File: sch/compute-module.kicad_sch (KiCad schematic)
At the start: 8 parts, among them J1 Conn_02x20_Odd_Even, J3 Conn_02x07_Odd_Even, SW1 SW_Push

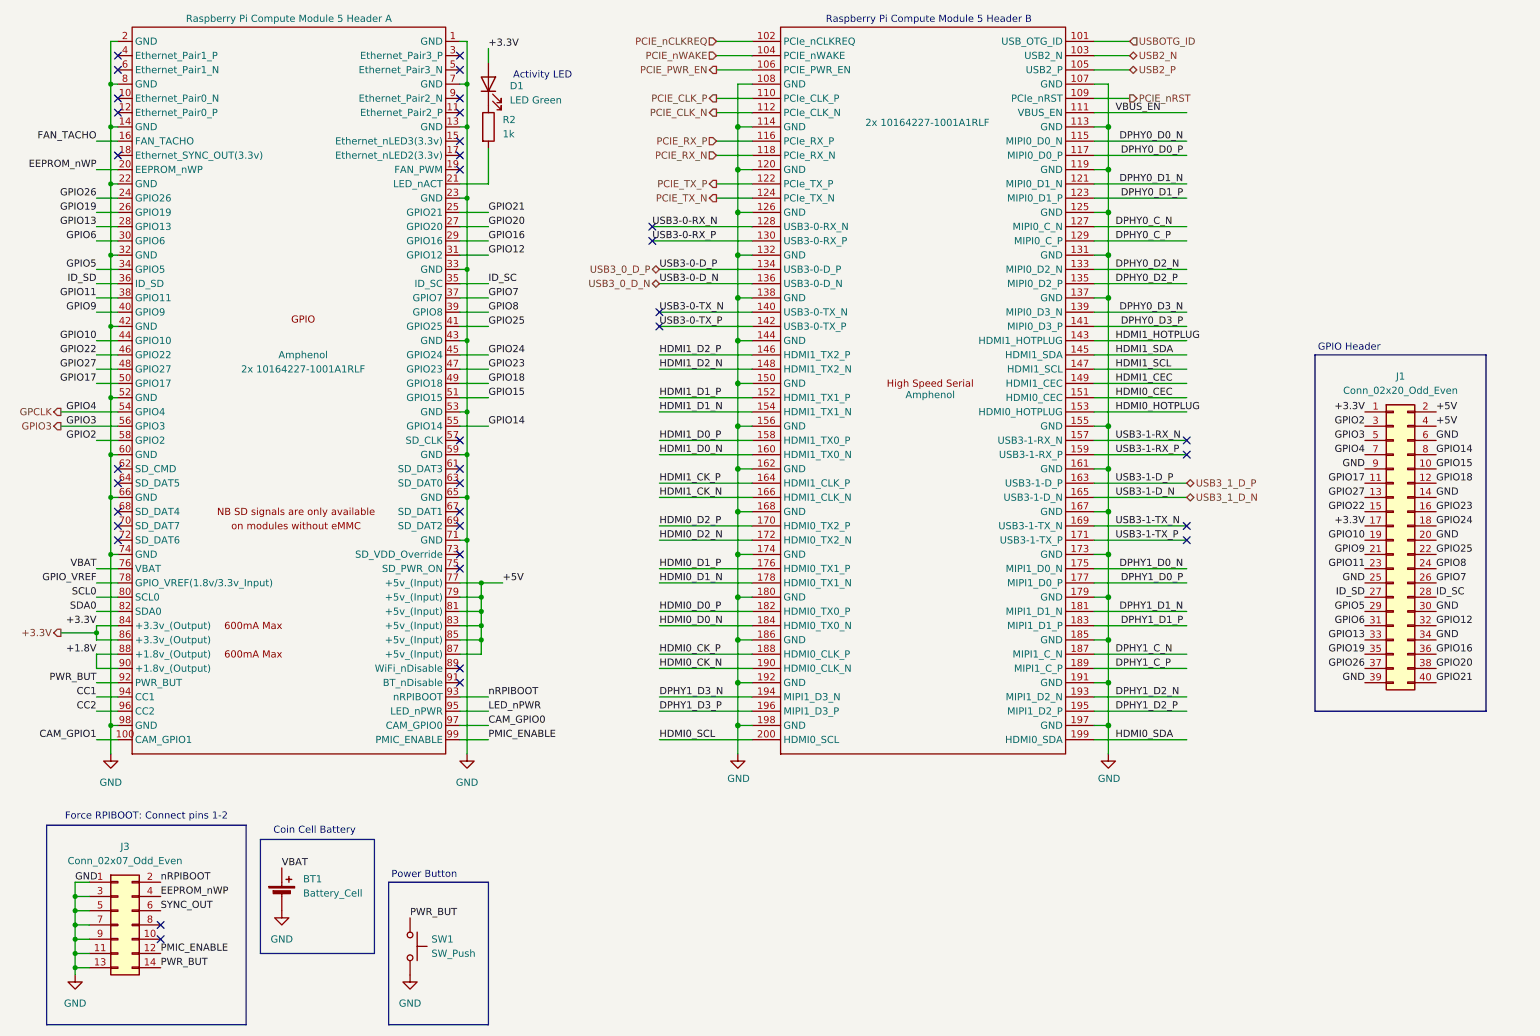
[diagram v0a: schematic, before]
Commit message: Connected pins between modem and CM5
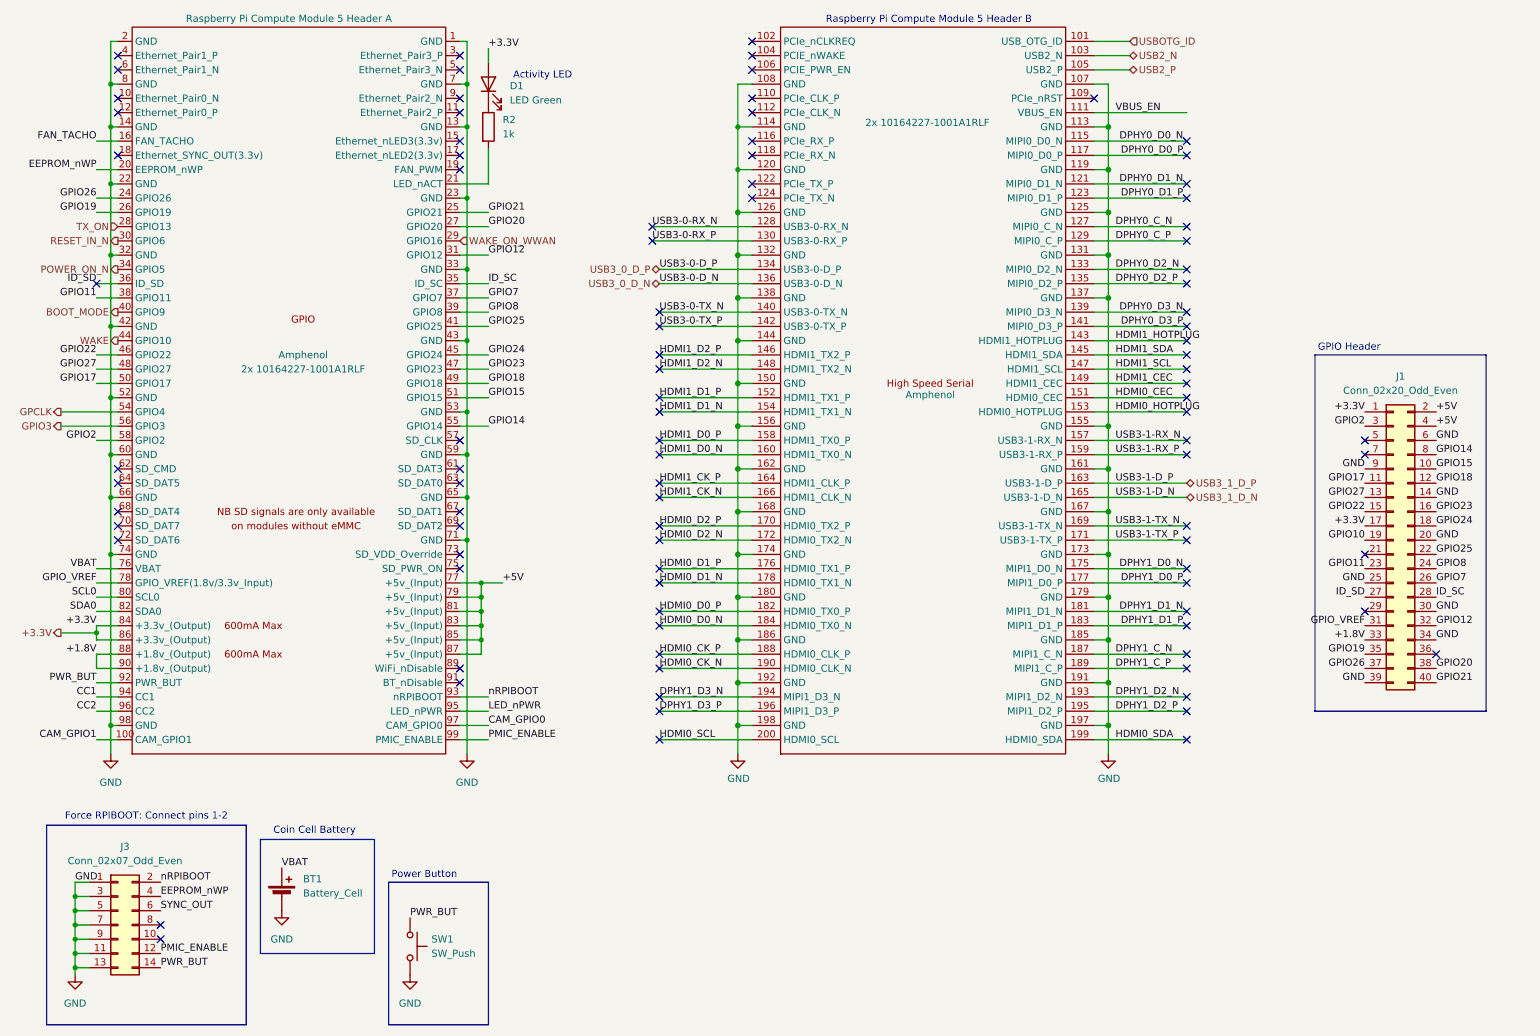
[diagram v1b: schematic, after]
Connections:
- net +1.8V: now also J1.33 (Pin_33)
- net GPCLK: no longer J1.7 (Pin_7)
- net GPIO10: no longer Module1.44 (GPIO10)
- net GPIO3: no longer J1.5 (Pin_5)
- net GPIO_VREF: now also J1.31 (Pin_31)
- net GPIO13 renamed TX_ON
- net TX_ON: no longer J1.33 (Pin_33)
- net GPIO16: no longer names the net of J1.36 (Pin_36)
- net GPIO16: no longer Module1.29 (GPIO16)
- net GPIO5: no longer names the net of J1.29 (Pin_29)
- net GPIO5: no longer Module1.34 (GPIO5)
- net GPIO6 renamed RESET_IN_N
- net RESET_IN_N: no longer J1.31 (Pin_31)
- net GPIO9: no longer names the net of J1.21 (Pin_21)
- net GPIO9: no longer Module1.40 (GPIO9)
- net PCIE_CLK_N: no longer names the net of Module2.112 (PCIe_CLK_N)
- net PCIE_CLK_P: no longer names the net of Module2.110 (PCIe_CLK_P)
- net PCIE_PWR_EN: no longer names the net of Module2.106 (PCIE_PWR_EN)
- net PCIE_RX_N: no longer names the net of Module2.118 (PCIe_RX_N)
- net PCIE_RX_P: no longer names the net of Module2.116 (PCIe_RX_P)
- net PCIE_TX_N: no longer names the net of Module2.124 (PCIe_TX_N)
- net PCIE_TX_P: no longer names the net of Module2.122 (PCIe_TX_P)
- net PCIE_nCLKREQ: no longer names the net of Module2.102 (PCIe_nCLKREQ)
- net PCIE_nRST: no longer names the net of Module2.109 (PCIe_nRST)
- net PCIE_nWAKE: no longer names the net of Module2.104 (PCIE_nWAKE)
- new net BOOT_MODE: Module1.40 (GPIO9)
- new net POWER_ON_N: Module1.34 (GPIO5)
- new net WAKE: Module1.44 (GPIO10)
- new net WAKE_ON_WWAN: Module1.29 (GPIO16)
- no-connect marks 36 -> 96

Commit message: Removed pin USBOTG
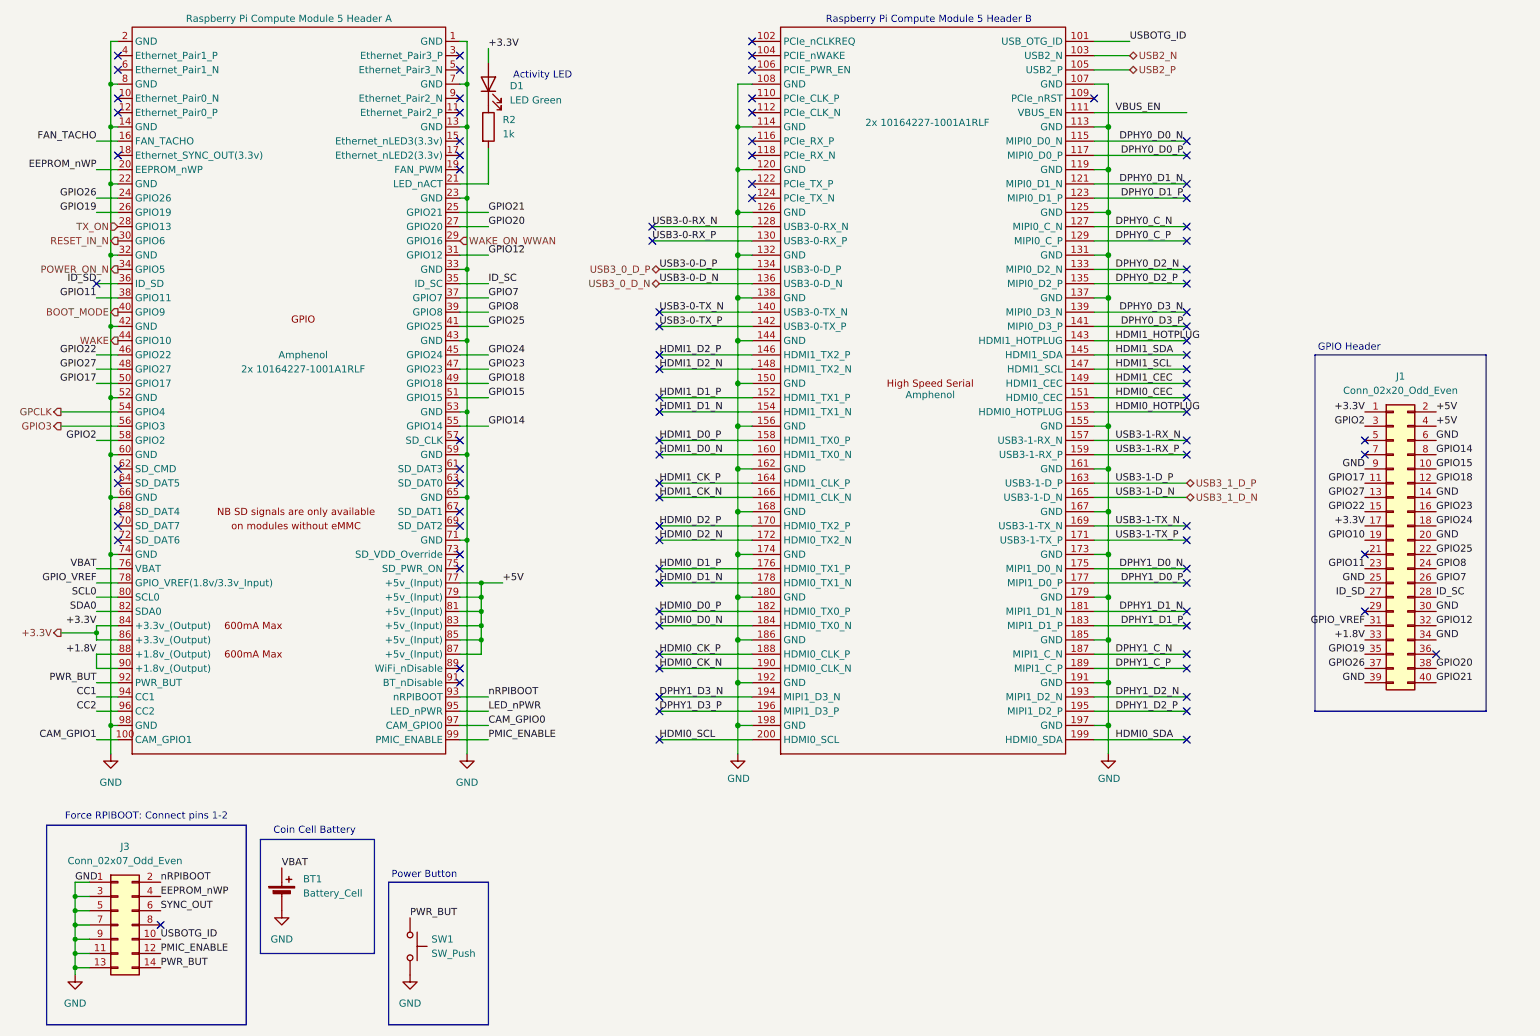
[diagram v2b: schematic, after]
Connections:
- net USBOTG_ID: now also J3.10 (Pin_10)
- no-connect marks 96 -> 95
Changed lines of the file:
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@@
 	)
 	(no_connect
-		(at 38.1 180.34)
-	)
-	(no_connect
 		(at 220.98 91.44)
 	)
@@
 		)
 	)
+	(label "USBOTG_ID"
+		(at 38.1 180.34 0)
+		(effects
+			(font
+				(size 1.27 1.27)
+			)
+			(justify left bottom)
+		)
+	)
 	(label "PWR_BUT"
 		(at 26.67 134.62 180)
@@
 		)
 	)
+	(label "USBOTG_ID"
+		(at 210.82 20.32 0)
+		(effects
+			(font
+				(size 1.27 1.27)
+			)
+			(justify left bottom)
+		)
+	)
 	(label "GPIO10"
 		(at 252.73 109.22 180)
@@
 		)
 	)
-	(hierarchical_label "USBOTG_ID"
-		(shape input)
-		(at 210.82 20.32 0)
-		(effects
-			(font
-				(size 1.27 1.27)
-			)
-			(justify left)
-		)
-	)
